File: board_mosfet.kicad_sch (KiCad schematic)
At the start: 14 parts, among them J2 USB_IN, J3 USB_OUT, J5 USB_OUT, Q1 Q_NMOS_GDS, Q2 Q_NMOS_GDS, U1 AMS1117-3.3, U2 INA219AxD, U3 INA219AxD

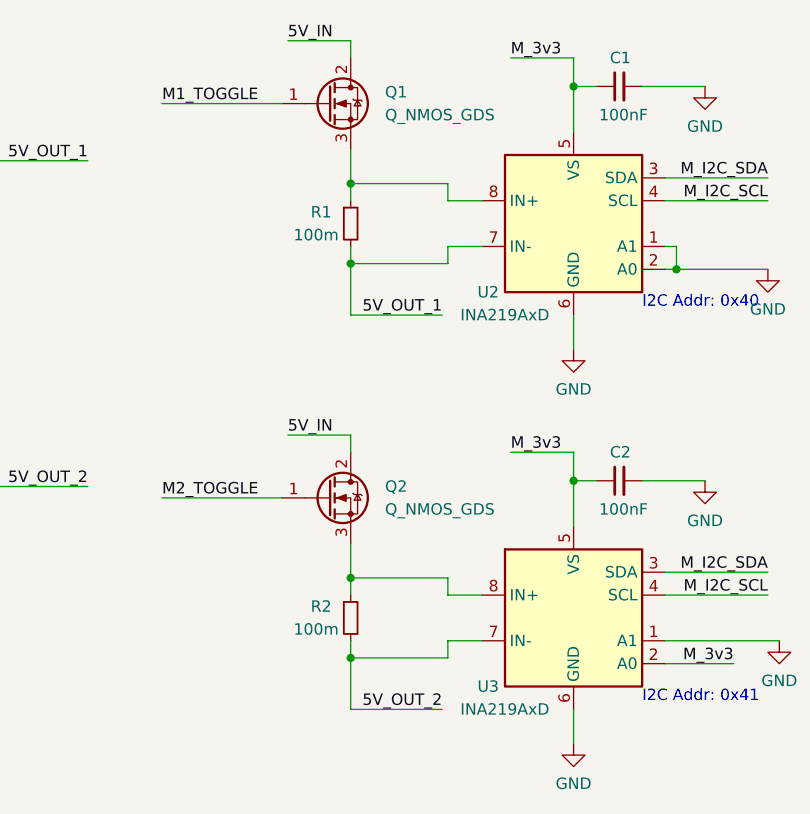
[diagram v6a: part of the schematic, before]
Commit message: Added more GND vias, fixed incorrect net trace sizing
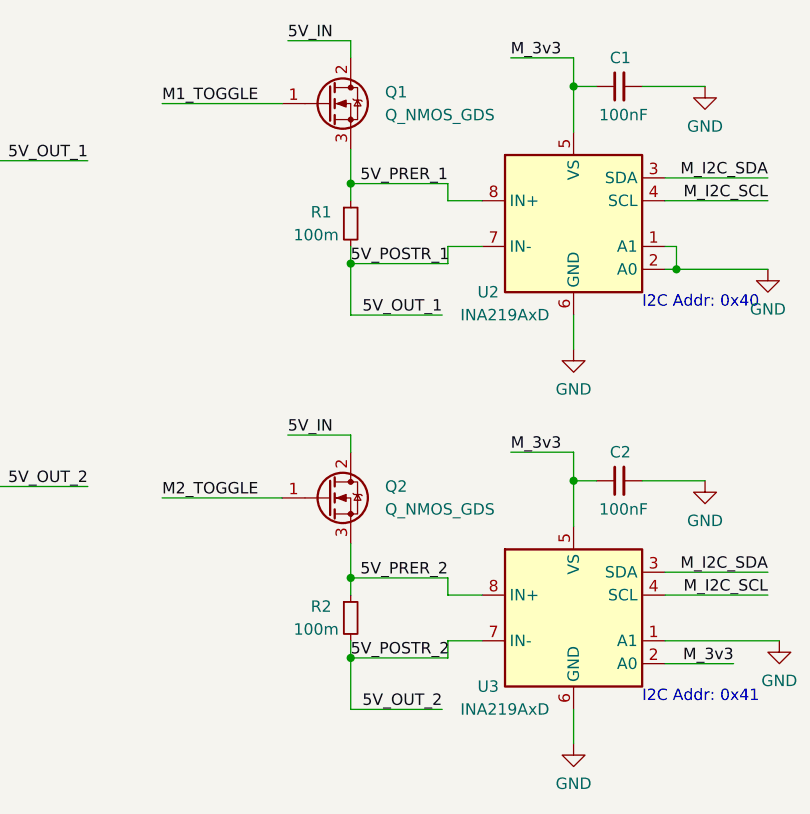
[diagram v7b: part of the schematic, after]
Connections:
- net 5V_PRER_2: now reaches Q2.3 (S), R2.1, U3.8 (IN+)
- net 5V_PRER_1: now reaches Q1.3 (S), R1.1, U2.8 (IN+)
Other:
- title: (none) -> Smart USB Port
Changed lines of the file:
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@@
 (kicad_sch (version 20211123) (generator eeschema)
   (paper "A4")
+  (title_block
+    (title "Smart USB Port")
+    (date "2022-10-23")
+    (rev "0.1")
+  )
   (junction (at 121.285 92.71) (diameter 0) (color 0 0 0 0)
   )
@@
     (effects (font (size 1.27 1.27)) (justify right bottom))
   )
+  (label "5V_PRER_1" (at 95.885 83.185 180)
+    (effects (font (size 1.27 1.27)) (justify right bottom))
+  )
   (label "5V_OUT_1" (at 95.25 97.79 180)
     (effects (font (size 1.27 1.27)) (justify right bottom))
@@
     (effects (font (size 1.27 1.27)) (justify right bottom))
   )
+  (label "5V_POSTR_2" (at 85.09 135.89 0)
+    (effects (font (size 1.27 1.27)) (justify left bottom))
+  )
   (label "M_I2C_SCL" (at 186.69 42.545 180)
     (effects (font (size 1.27 1.27)) (justify right bottom))
@@
     (effects (font (size 1.27 1.27)) (justify left bottom))
   )
+  (label "5V_PRER_2" (at 95.885 127 180)
+    (effects (font (size 1.27 1.27)) (justify right bottom))
+  )
   (label "M_I2C_SCL" (at 131.445 85.09 180)
     (effects (font (size 1.27 1.27)) (justify right bottom))
   )
+  (label "5V_POSTR_1" (at 85.09 92.075 0)
+    (effects (font (size 1.27 1.27)) (justify left bottom))
+  )
   (hierarchical_label "GND" (shape bidirectional) (at 198.12 46.99 180)

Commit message: Updated some components to use ones I already own
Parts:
- C1, C2: LCSC Part Number C30926 -> C1591; Manufacturer FH (Guangdong Fenghua Advanced Tech) -> Samsung Electro-Mechanics; Manufacturer Part Number 0603B104K500NT -> CL10B104KB8NNNC
- C5, C6: LCSC Part Number C100042 -> C19702; Manufacturer YAGEO -> Samsung Electro-Mechanics; Manufacturer Part Number CC0603KRX7R9BB103 -> CL10A106KP8NNNC
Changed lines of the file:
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@@
       (effects (font (size 1.27 1.27)) hide)
     )
-    (property "LCSC Part Number" "C30926" (id 4) (at 114.935 116.205 0)
+    (property "LCSC Part Number" "C1591" (id 4) (at 114.935 116.205 0)
       (effects (font (size 1.27 1.27)) hide)
     )
-    (property "Manufacturer" "FH (Guangdong Fenghua Advanced Tech)" (id 5) (at 114.935 116.205 0)
+    (property "Manufacturer" "Samsung Electro-Mechanics" (id 5) (at 114.935 116.205 0)
       (effects (font (size 1.27 1.27)) hide)
     )
-    (property "Manufacturer Part Number" "0603B104K500NT" (id 6) (at 114.935 116.205 0)
+    (property "Manufacturer Part Number" "CL10B104KB8NNNC" (id 6) (at 114.935 116.205 0)
       (effects (font (size 1.27 1.27)) hide)
     )
@@
       (effects (font (size 1.27 1.27)) hide)
     )
-    (property "LCSC Part Number" "C100042" (id 4) (at 81.28 47.625 0)
+    (property "LCSC Part Number" "C19702" (id 4) (at 81.28 47.625 0)
       (effects (font (size 1.27 1.27)) hide)
     )
-    (property "Manufacturer" "YAGEO" (id 5) (at 81.28 47.625 0)
+    (property "Manufacturer" "Samsung Electro-Mechanics" (id 5) (at 81.28 47.625 0)
       (effects (font (size 1.27 1.27)) hide)
     )
-    (property "Manufacturer Part Number" "CC0603KRX7R9BB103" (id 6) (at 81.28 47.625 0)
+    (property "Manufacturer Part Number" "CL10A106KP8NNNC" (id 6) (at 81.28 47.625 0)
       (effects (font (size 1.27 1.27)) hide)
     )
@@
       (effects (font (size 1.27 1.27)) hide)
     )
-    (property "LCSC Part Number" "C30926" (id 4) (at 114.935 72.39 0)
+    (property "LCSC Part Number" "C1591" (id 4) (at 114.935 72.39 0)
       (effects (font (size 1.27 1.27)) hide)
     )
-    (property "Manufacturer" "FH (Guangdong Fenghua Advanced Tech)" (id 5) (at 114.935 72.39 0)
+    (property "Manufacturer" "Samsung Electro-Mechanics" (id 5) (at 114.935 72.39 0)
       (effects (font (size 1.27 1.27)) hide)
     )
-    (property "Manufacturer Part Number" "0603B104K500NT" (id 6) (at 114.935 72.39 0)
+    (property "Manufacturer Part Number" "CL10B104KB8NNNC" (id 6) (at 114.935 72.39 0)
       (effects (font (size 1.27 1.27)) hide)
     )
@@
       (effects (font (size 1.27 1.27)) hide)
     )
-    (property "LCSC Part Number" "C100042" (id 4) (at 104.775 47.625 0)
+    (property "LCSC Part Number" "C19702" (id 4) (at 104.775 47.625 0)
       (effects (font (size 1.27 1.27)) hide)
     )
-    (property "Manufacturer" "YAGEO" (id 5) (at 104.775 47.625 0)
+    (property "Manufacturer" "Samsung Electro-Mechanics" (id 5) (at 104.775 47.625 0)
       (effects (font (size 1.27 1.27)) hide)
     )
-    (property "Manufacturer Part Number" "CC0603KRX7R9BB103" (id 6) (at 104.775 47.625 0)
+    (property "Manufacturer Part Number" "CL10A106KP8NNNC" (id 6) (at 104.775 47.625 0)
       (effects (font (size 1.27 1.27)) hide)
     )
